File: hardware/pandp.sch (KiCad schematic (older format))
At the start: 88 parts, among them IC1 ADP2303-5, P1 CONN_01X02, P10 CONN_01X04, P11 CONN_01X02, P12 CONN_02X04, P13 CONN_01X02, P14 CONN_01X04, P15 CONN_01X04, P16 CONN_01X03, P17 CONN_01X03, P18 CONN_01X03, P19 CONN_01X03, P2 CONN_01X03, P20 CONN_01X03, P21 CONN_01X03, P22 CONN_02X03, P23 CONN_02X03, P24 CONN_02X03, P25 CONN_02X03, P26 CONN_01X03, P27 CONN_01X03, P28 CONN_01X03, P29 CONN_01X03, P3 CONN_01X02, P30 CONN_01X04, P31 CONN_01X04, P32 CONN_01X04, P33 CONN_01X04, P4 CONN_01X03, P6 CONN_01X03, P7 CONN_01X03, P8 USB_OTG, P9 CONN_01X02, Q1 IRF540N, Q2 IRF540N, SW1 SW_PUSH, U1 AP1117D33, U2 STM32F103RC, Y1 Crystal_Small - 2101357 on el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, Y2 Crystal_Small - 2063972 on el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

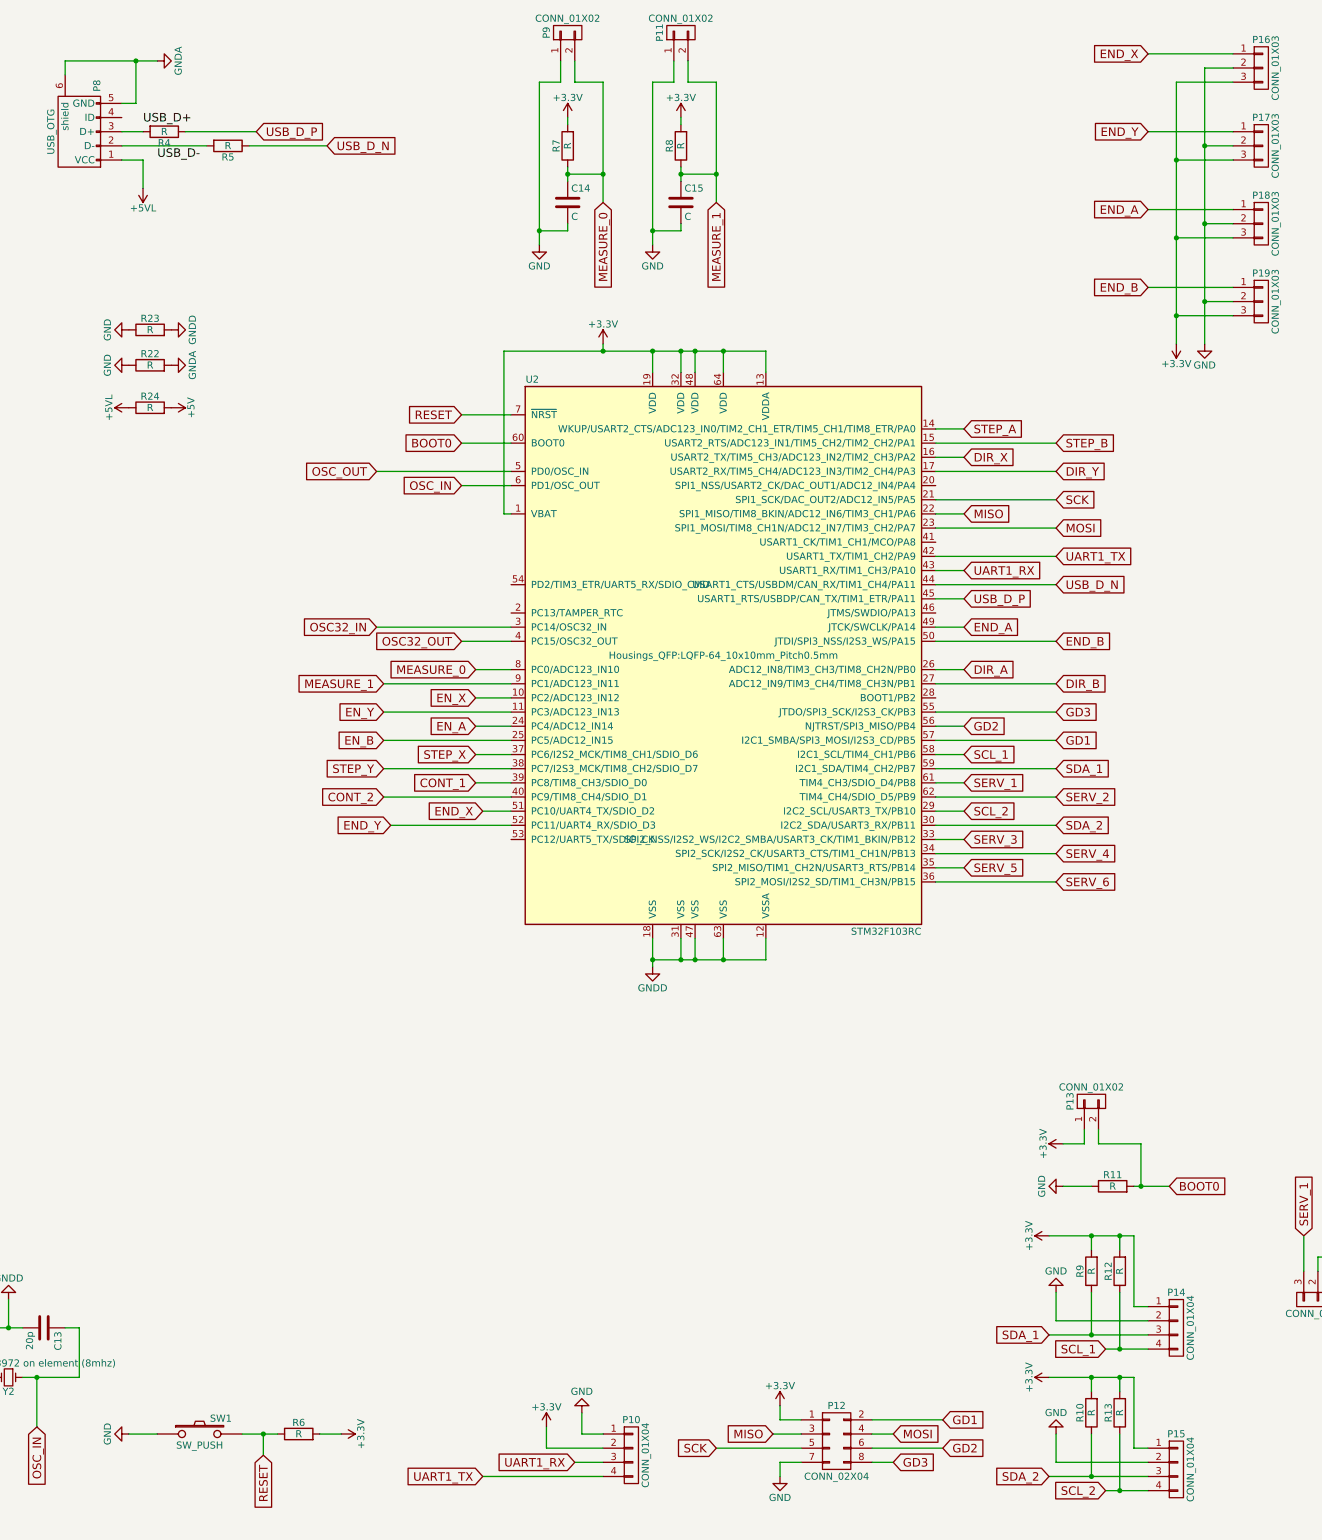
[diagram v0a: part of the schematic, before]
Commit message: added 5v dc motor control - low current - 500ma or less
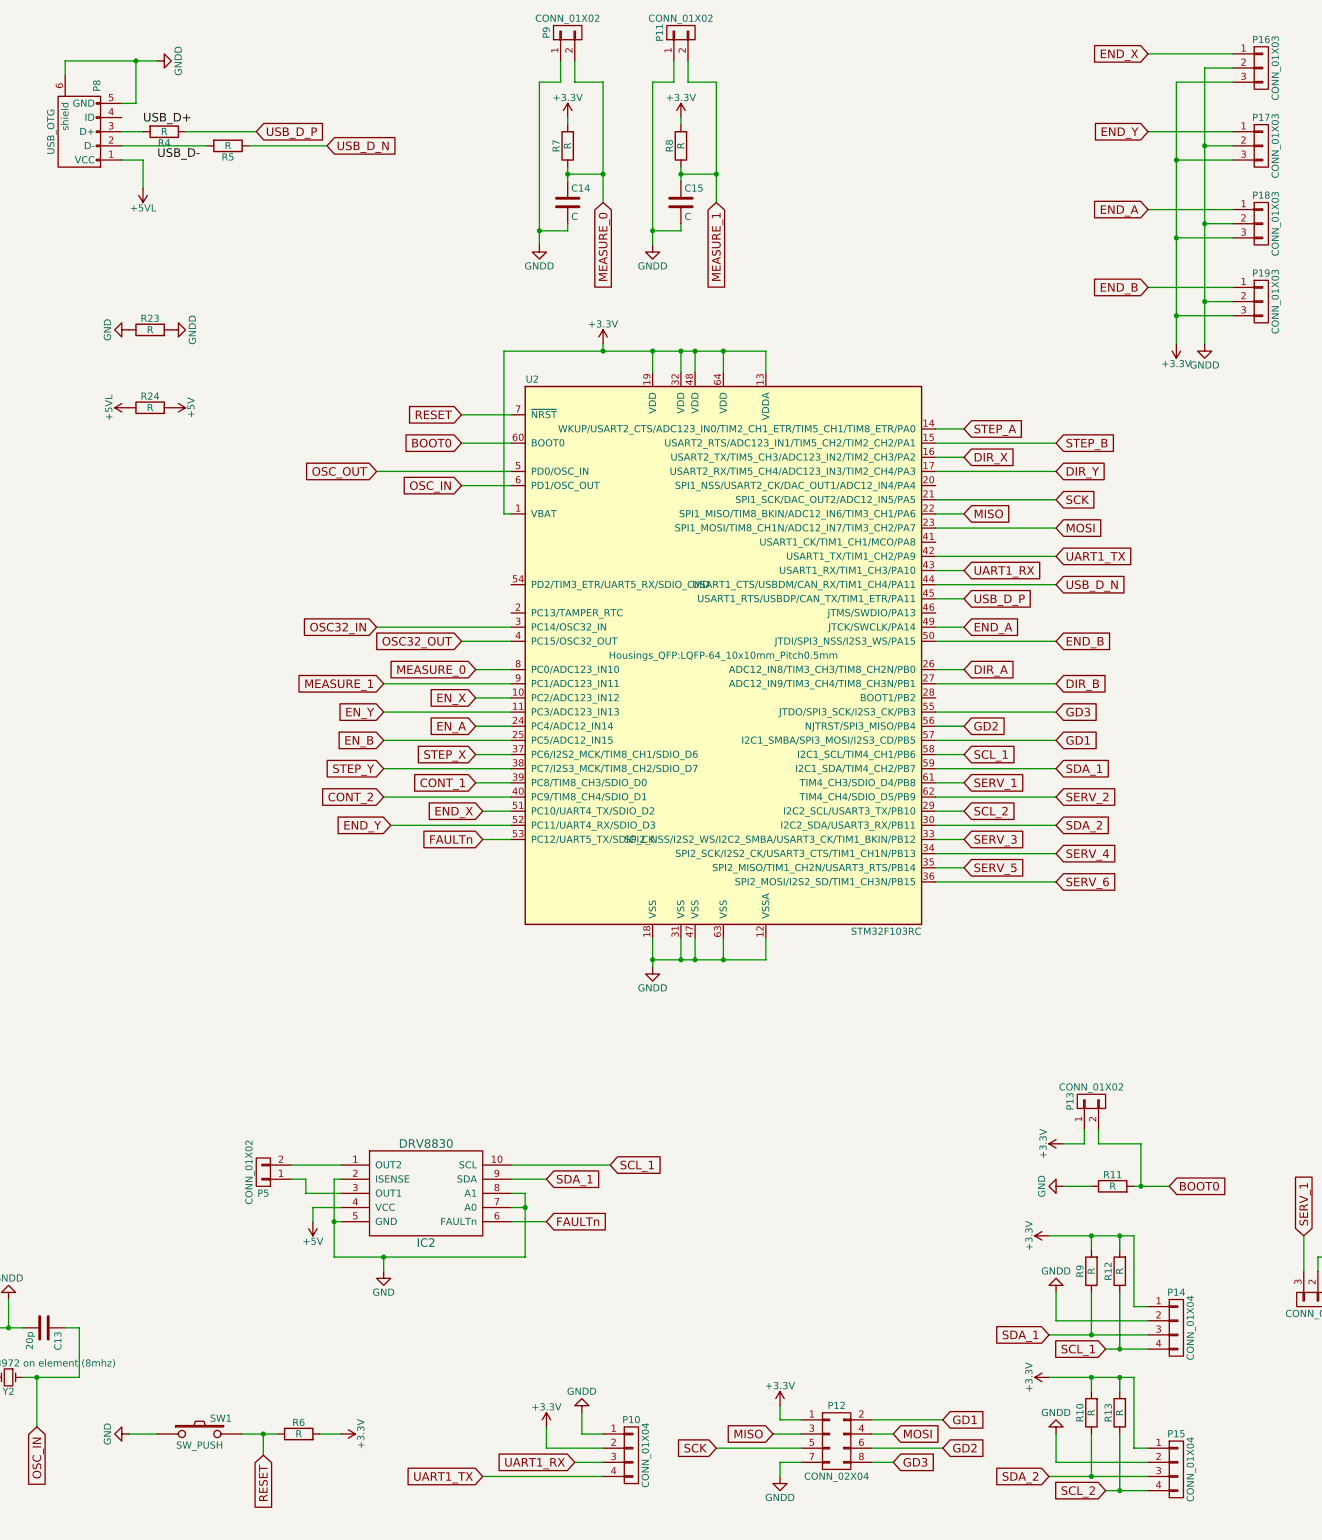
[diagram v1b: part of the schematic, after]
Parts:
- removed R22: R, Resistors_SMD:R_0402, symbol R
- added IC2: DRV8830, Housings_SSOP:TSSOP-10_3x3mm_Pitch0.5mm, symbol DRV8830
- added P5: CONN_01X02, Pin_Headers:Pin_Header_Straight_1x02, symbol CONN_01X02
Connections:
- net GNDA is gone; now on net GNDD: P8.5 (GND), P8.6 (shield)
- net +5V: now also IC2.4 (VCC)
- net GND: now also IC2.2 (ISENSE), IC2.5 (GND), IC2.7 (A0), IC2.8 (A1); no longer C14.2, C15.2, P10.1 (P1), P11.1 (P1), P12.7 (P7), P14.2 (P2), P15.2 (P2), P16.2 (P2), P17.2 (P2), P18.2 (P2), P19.2 (P2), P9.1 (P1)
- net GNDD: now also C14.2, C15.2, P10.1 (P1), P11.1 (P1), P12.7 (P7), P14.2 (P2), P15.2 (P2), P16.2 (P2), P17.2 (P2), P18.2 (P2), P19.2 (P2), P9.1 (P1)
- net SCL_1: now also IC2.10 (SCL)
- net SDA_1: now also IC2.9 (SDA)
- net FAULTn: now reaches U2.53 (PC12/UART5_TX/SDIO_CK)
- net FAULTn: now also IC2.6 (FAULTn)
- new net: IC2.1 (OUT2), P5.2 (P2)
- new net: IC2.3 (OUT1), P5.1 (P1)

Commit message: new uusb oshpark compatible, added a mark for the stm chip pin 0
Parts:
- P8: footprint Connect:USB_Micro-B -> MyLibs:USB_Micro-B-OshPark
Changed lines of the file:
@@
 F 0 "P8" H 4075 1225 50  0000 C CNN
 F 1 "USB_OTG" H 3750 1550 50  0000 C CNN
-F 2 "Connect:USB_Micro-B" V 3700 1250 50  0001 C CNN
+F 2 "MyLibs:USB_Micro-B-OshPark" V 3700 1250 50  0001 C CNN
 F 3 "" V 3700 1250 50  0000 C CNN
 	1    3750 1350
@@
 $EndComp
 $Comp
-L +5V #PWR051
+L +5V #PWR048
 U 1 1 57F66656
 P 850 850
-F 0 "#PWR051" H 850 700 50  0001 C CNN
+F 0 "#PWR048" H 850 700 50  0001 C CNN
 F 1 "+5V" H 850 990 50  0000 C CNN
 F 2 "" H 850 850 50  0000 C CNN
@@
 5V_IND
 $Comp
-L +12V #PWR052
+L +12V #PWR049
 U 1 1 57F67DAB
 P 2300 6950
-F 0 "#PWR052" H 2300 6800 50  0001 C CNN
+F 0 "#PWR049" H 2300 6800 50  0001 C CNN
 F 1 "+12V" H 2300 7090 50  0000 C CNN
 F 2 "" H 2300 6950 50  0000 C CNN
@@
 $EndComp
 $Comp
-L GNDD #PWR053
+L GNDD #PWR050
 U 1 1 57F5E959
 P 1500 9600
-F 0 "#PWR053" H 1500 9350 50  0001 C CNN
+F 0 "#PWR050" H 1500 9350 50  0001 C CNN
 F 1 "GNDD" H 1500 9450 50  0000 C CNN
 F 2 "" H 1500 9600 50  0000 C CNN
@@
 $EndComp
 $Comp
-L GNDD #PWR054
+L GNDD #PWR051
 U 1 1 57F5EA6F
 P 3250 9600
-F 0 "#PWR054" H 3250 9350 50  0001 C CNN
+F 0 "#PWR051" H 3250 9350 50  0001 C CNN
 F 1 "GNDD" H 3250 9450 50  0000 C CNN
 F 2 "" H 3250 9600 50  0000 C CNN
@@
 $EndComp
 $Comp
-L +5V #PWR055
+L +5V #PWR052
 U 1 1 57F675CA
 P 4400 3300
-F 0 "#PWR055" H 4400 3150 50  0001 C CNN
+F 0 "#PWR052" H 4400 3150 50  0001 C CNN
 F 1 "+5V" H 4400 3440 50  0000 C CNN
 F 2 "" H 4400 3300 50  0000 C CNN
@@
 $EndComp
 $Comp
-L +5VL #PWR056
+L +5VL #PWR053
 U 1 1 57F676E2
 P 4100 3300
-F 0 "#PWR056" H 4100 3150 50  0001 C CNN
+F 0 "#PWR053" H 4100 3150 50  0001 C CNN
 F 1 "+5VL" H 4100 3440 50  0000 C CNN
 F 2 "" H 4100 3300 50  0000 C CNN
@@
 $EndComp
 $Comp
-L +5VL #PWR057
+L +5VL #PWR054
 U 1 1 57F67855
 P 4200 1750
-F 0 "#PWR057" H 4200 1600 50  0001 C CNN
+F 0 "#PWR054" H 4200 1600 50  0001 C CNN
 F 1 "+5VL" H 4200 1890 50  0000 C CNN
 F 2 "" H 4200 1750 50  0000 C CNN
@@
 SCL_1
 $Comp
-L +5V #PWR058
+L +5V #PWR055
 U 1 1 57FBD27A
 P 5400 9050
-F 0 "#PWR058" H 5400 8900 50  0001 C CNN
+F 0 "#PWR055" H 5400 8900 50  0001 C CNN
 F 1 "+5V" H 5400 9190 50  0000 C CNN
 F 2 "" H 5400 9050 50  0000 C CNN
@@
 Connection ~ 6900 8950
 $Comp
-L GND #PWR059
+L GND #PWR056
 U 1 1 57FC4EB3
 P 5900 9400
-F 0 "#PWR059" H 5900 9150 50  0001 C CNN
+F 0 "#PWR056" H 5900 9150 50  0001 C CNN
 F 1 "GND" H 5900 9250 50  0000 C CNN
 F 2 "" H 5900 9400 50  0000 C CNN
@@
 $EndComp
 $Comp
-L GNDD #PWR060
+L GNDD #PWR057
 U 1 1 57FC5392
 P 7300 10400
-F 0 "#PWR060" H 7300 10150 50  0001 C CNN
+F 0 "#PWR057" H 7300 10150 50  0001 C CNN
 F 1 "GNDD" H 7300 10250 50  0000 C CNN
 F 2 "" H 7300 10400 50  0000 C CNN
@@
 $EndComp
 $Comp
-L GNDD #PWR061
+L GNDD #PWR058
 U 1 1 57FC561E
 P 8700 10850
-F 0 "#PWR061" H 8700 10600 50  0001 C CNN
+F 0 "#PWR058" H 8700 10600 50  0001 C CNN
 F 1 "GNDD" H 8700 10700 50  0000 C CNN
 F 2 "" H 8700 10850 50  0000 C CNN
@@
 $EndComp
 $Comp
-L GNDD #PWR062
+L GNDD #PWR059
 U 1 1 57FC57ED
 P 10650 10550
-F 0 "#PWR062" H 10650 10300 50  0001 C CNN
+F 0 "#PWR059" H 10650 10300 50  0001 C CNN
 F 1 "GNDD" H 10650 10400 50  0000 C CNN
 F 2 "" H 10650 10550 50  0000 C CNN
@@
 $EndComp
 $Comp
-L GNDD #PWR063
+L GNDD #PWR060
 U 1 1 57FC5906
 P 10650 9550
-F 0 "#PWR063" H 10650 9300 50  0001 C CNN
+F 0 "#PWR060" H 10650 9300 50  0001 C CNN
 F 1 "GNDD" H 10650 9400 50  0000 C CNN
 F 2 "" H 10650 9550 50  0000 C CNN
@@
 $EndComp
 $Comp
-L GNDD #PWR064
+L GNDD #PWR061
 U 1 1 57FC5E09
 P 7800 2150
-F 0 "#PWR064" H 7800 1900 50  0001 C CNN
+F 0 "#PWR061" H 7800 1900 50  0001 C CNN
 F 1 "GNDD" H 7800 2000 50  0000 C CNN
 F 2 "" H 7800 2150 50  0000 C CNN
@@
 $EndComp
 $Comp
-L GNDD #PWR065
+L GNDD #PWR062
 U 1 1 57FC5F22
 P 7000 2150
-F 0 "#PWR065" H 7000 1900 50  0001 C CNN
+F 0 "#PWR062" H 7000 1900 50  0001 C CNN
 F 1 "GNDD" H 7000 2000 50  0000 C CNN
 F 2 "" H 7000 2150 50  0000 C CNN
@@
 $EndComp
 $Comp
-L GNDD #PWR066
+L GNDD #PWR063
 U 1 1 57FC6298
 P 11700 2850
-F 0 "#PWR066" H 11700 2600 50  0001 C CNN
+F 0 "#PWR063" H 11700 2600 50  0001 C CNN
 F 1 "GNDD" H 11700 2700 50  0000 C CNN
 F 2 "" H 11700 2850 50  0000 C CNN
@@
 $EndComp
 $Comp
-L GNDD #PWR?
+L GNDD #PWR064
 U 1 1 57FC6A8A
 P 4300 850
-F 0 "#PWR?" H 4300 600 50  0001 C CNN
+F 0 "#PWR064" H 4300 600 50  0001 C CNN
 F 1 "GNDD" H 4300 700 50  0000 C CNN
 F 2 "" H 4300 850 50  0000 C CNN

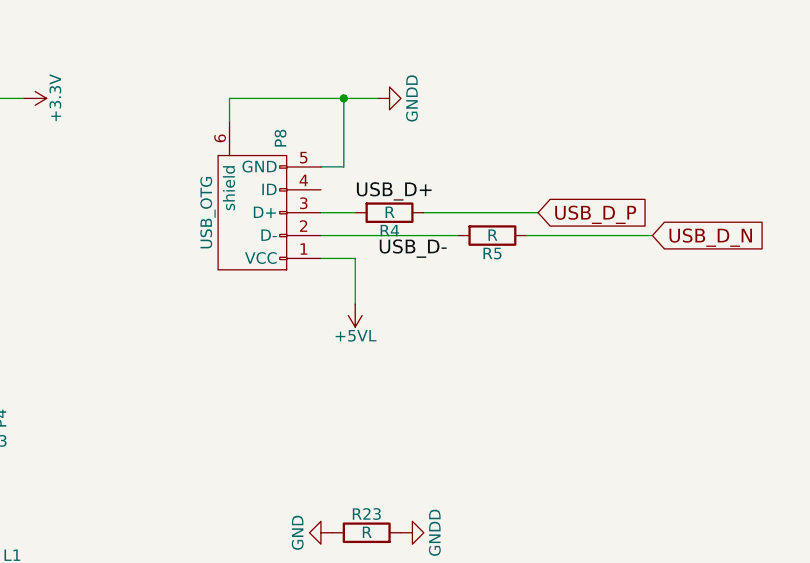
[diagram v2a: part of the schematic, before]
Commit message: added pullup for usb
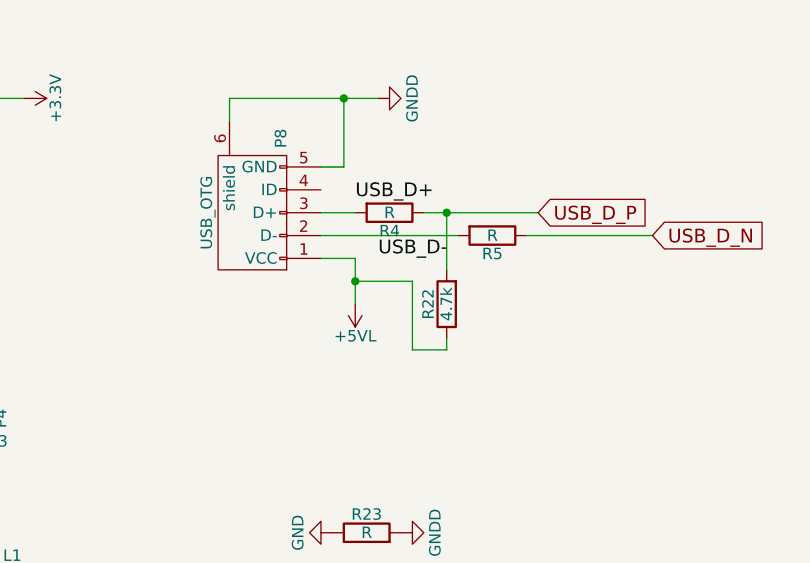
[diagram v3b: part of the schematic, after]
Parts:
- added R22: 4.7k, Resistors_SMD:R_0805_HandSoldering, symbol R
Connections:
- net +5VL: now also R22.1
- net USB_D_P: now also R22.2
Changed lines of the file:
@@
 	0    -1   -1   0
 $EndComp
+$Comp
+L R R22
+U 1 1 58029668
+P 4600 1750
+F 0 "R22" V 4680 1750 50  0000 C CNN
+F 1 "4.7k" V 4600 1750 50  0000 C CNN
+F 2 "Resistors_SMD:R_0805_HandSoldering" V 4530 1750 50  0001 C CNN
+F 3 "" H 4600 1750 50  0000 C CNN
+	1    4600 1750
+	-1   0    0    1
+$EndComp
+Wire Wire Line
+	4600 1600 4600 1350
+Connection ~ 4600 1350
+Wire Wire Line
+	4600 1900 4600 1950
+Wire Wire Line
+	4600 1950 4450 1950
+Wire Wire Line
+	4450 1950 4450 1650
+Wire Wire Line
+	4450 1650 4200 1650
+Connection ~ 4200 1650
 $EndSCHEMATC
